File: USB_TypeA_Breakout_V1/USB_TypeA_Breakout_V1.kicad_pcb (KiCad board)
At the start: 2 copper layers, 27 x 20 mm, 2 parts, among them J1 USB_A, J2 Conn_01x04_Male

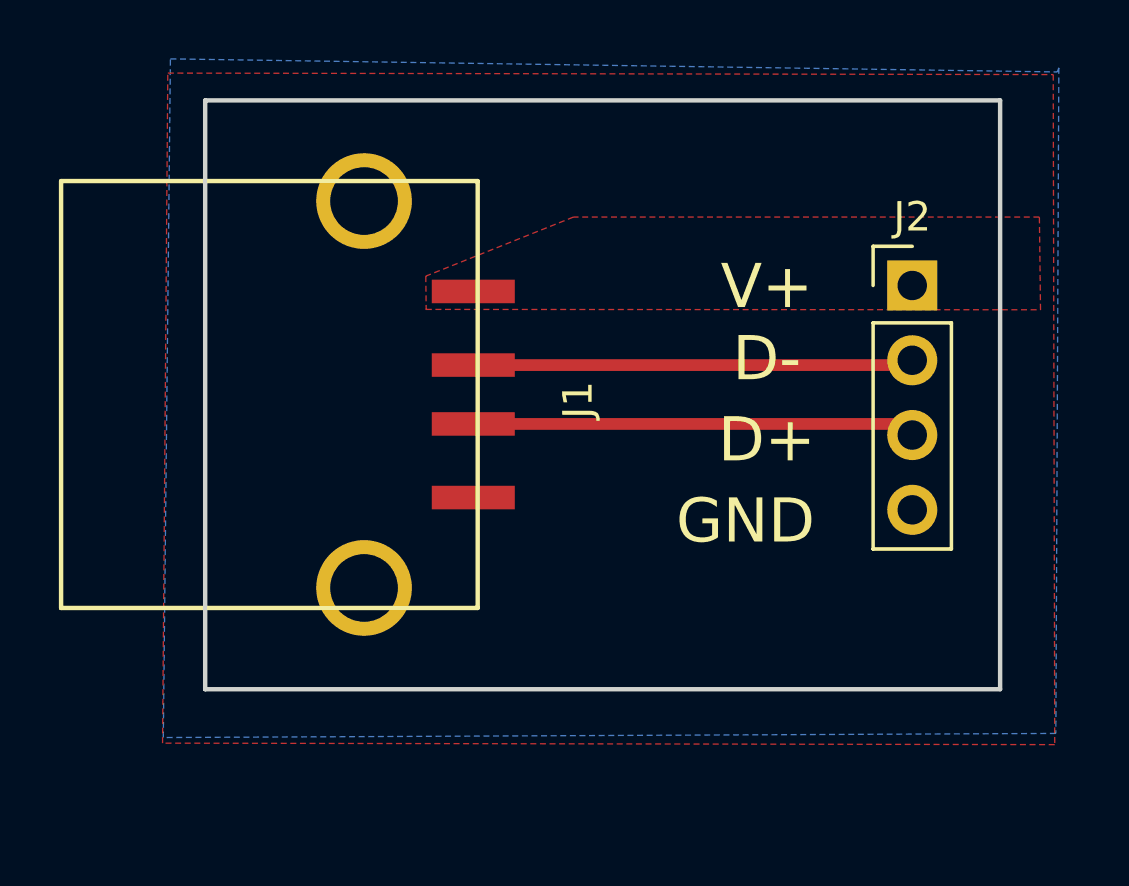
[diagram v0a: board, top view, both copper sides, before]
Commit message: Added rounded corners to PCB layout.
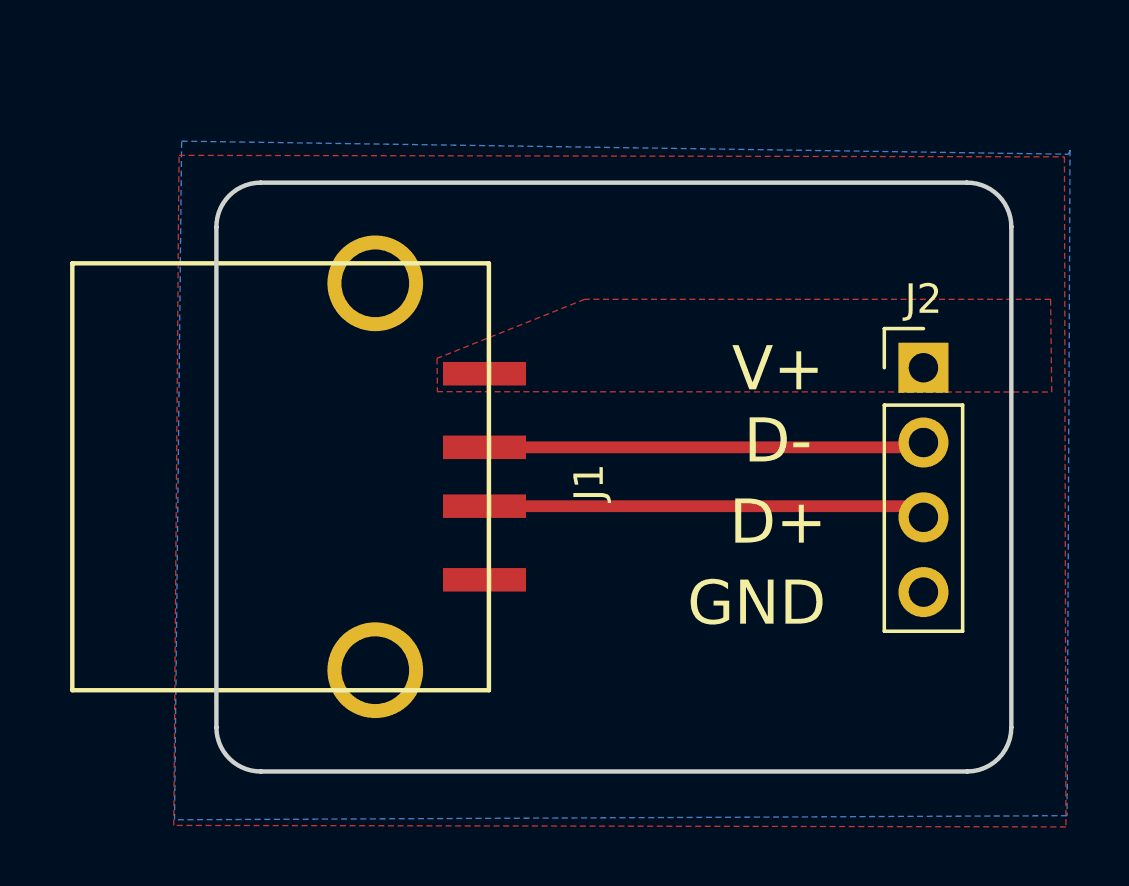
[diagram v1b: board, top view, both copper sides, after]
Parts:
- moved J1 2.82 mm to (121.5, 80.8)
- moved J2 2.82 mm to (136.4, 80.6)
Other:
- outline, holes or cut-outs redrawn
- board text added: "USB Type A Breakout V1"
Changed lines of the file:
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@@
   (general
     (thickness 1.6)
-    (drawings 8)
+    (drawings 13)
     (tracks 4)
     (zones 0)
@@
   )
   (module Custom_Footprints:USB_A_CNC_1002-002-01100 (layer F.Cu)
-    (at 121.158 78.0034 270)
+    (at 121.539 80.7974 270)
     (fp_text reference J1 (at 3.683 -3.556 270) (layer F.SilkS)
       (effects (font (size 1 1) (thickness 0.15)))
@@
   )
   (module Connector_PinHeader_2.54mm:PinHeader_1x04_P2.54mm_Vertical (layer F.Cu)
-    (at 136.0678 77.8002)
+    (at 136.4488 80.5942)
     (descr "Through hole straight pin header, 1x04, 2.54mm pitch, single row")
     (tags "Through hole pin header THT 1x04 2.54mm single row")
@@
     )
   )
-  (gr_line (start 112.0521 71.5137) (end 139.0521 71.5137) (layer Edge.Cuts) (width 0.15))
-  (gr_line (start 139.0521 71.5137) (end 139.0521 91.5137) (layer Edge.Cuts) (width 0.15))
-  (gr_line (start 139.0521 91.5137) (end 112.0521 91.5137) (layer Edge.Cuts) (width 0.15))
-  (gr_line (start 112.0521 91.5137) (end 112.0521 71.5137) (layer Edge.Cuts) (width 0.15))
-  (gr_text GND (at 130.4036 85.8012) (layer F.SilkS)
-    (effects (font (size 1.5 1.5) (thickness 0.3)))
-  )
-  (gr_text D+ (at 131.1275 83.0453) (layer F.SilkS)
-    (effects (font (size 1.5 1.5) (thickness 0.3)))
-  )
-  (gr_text D- (at 131.1275 80.2894) (layer F.SilkS)
-    (effects (font (size 1.5 1.5) (thickness 0.3)))
-  )
-  (gr_text V+ (at 131.1275 77.8383) (layer F.SilkS)
-    (effects (font (size 1.5 1.5) (thickness 0.3)))
-  )
-  (segment (start 135.9046 80.5034) (end 136.0678 80.3402) (width 0.25) (layer F.Cu) (net 2))
-  (segment (start 121.158 80.5034) (end 135.9046 80.5034) (width 0.4) (layer F.Cu) (net 2))
-  (segment (start 135.691 82.5034) (end 136.0678 82.8802) (width 0.25) (layer F.Cu) (net 3))
-  (segment (start 121.158 82.5034) (end 135.691 82.5034) (width 0.4) (layer F.Cu) (net 3))
+  (gr_text "USB Type A\nBreakout V1" (at 126.9238 84.201 90) (layer B.SilkS)
+    (effects (font (size 1.5 1.5) (thickness 0.3)) (justify mirror))
+  )
+  (gr_arc (start 113.9331 75.8077) (end 113.9331 74.3077) (angle -90.43174927) (layer Edge.Cuts) (width 0.15))
+  (gr_arc (start 113.9331 92.8077) (end 112.4331 92.8077) (angle -90.5) (layer Edge.Cuts) (width 0.15))
+  (gr_arc (start 137.9331 75.8077) (end 139.4331 75.8077) (angle -90.42410656) (layer Edge.Cuts) (width 0.15))
+  (gr_arc (start 137.9331 92.8077) (end 137.9331 94.3077) (angle -89.9) (layer Edge.Cuts) (width 0.15))
+  (gr_line (start 113.9331 74.3077) (end 137.921997 74.3077) (layer Edge.Cuts) (width 0.15))
+  (gr_line (start 139.4331 75.8077) (end 139.4331 92.80906) (layer Edge.Cuts) (width 0.15))
+  (gr_line (start 137.9331 94.3077) (end 113.94619 94.3077) (layer Edge.Cuts) (width 0.15))
+  (gr_line (start 112.4331 92.8077) (end 112.4331 75.819003) (layer Edge.Cuts) (width 0.15))
+  (gr_text GND (at 130.7846 88.5952) (layer F.SilkS)
+    (effects (font (size 1.5 1.5) (thickness 0.3)))
+  )
+  (gr_text D+ (at 131.5085 85.8393) (layer F.SilkS)
+    (effects (font (size 1.5 1.5) (thickness 0.3)))
+  )
+  (gr_text D- (at 131.5085 83.0834) (layer F.SilkS)
+    (effects (font (size 1.5 1.5) (thickness 0.3)))
+  )
+  (gr_text V+ (at 131.5085 80.6323) (layer F.SilkS)
+    (effects (font (size 1.5 1.5) (thickness 0.3)))
+  )
+  (segment (start 136.2856 83.2974) (end 136.4488 83.1342) (width 0.25) (layer F.Cu) (net 2))
+  (segment (start 121.539 83.2974) (end 136.2856 83.2974) (width 0.4) (layer F.Cu) (net 2))
+  (segment (start 136.072 85.2974) (end 136.4488 85.6742) (width 0.25) (layer F.Cu) (net 3))
+  (segment (start 121.539 85.2974) (end 136.072 85.2974) (width 0.4) (layer F.Cu) (net 3))
   (zone (net 1) (net_name "Net-(J1-Pad1)") (layer F.Cu) (hatch edge 0.508)
     (priority 1)
@@
     (polygon
       (pts
-        (xy 119.5451 78.613) (xy 140.4239 78.6257) (xy 140.3858 75.4761) (xy 124.5616 75.4761) (xy 119.5451 77.4827)
-        (xy 119.5578 78.613)
+        (xy 119.9261 81.407) (xy 140.8049 81.4197) (xy 140.7668 78.2701) (xy 124.9426 78.2701) (xy 119.9261 80.2767)
+        (xy 119.9388 81.407)
       )
     )
@@
     (polygon
       (pts
-        (xy 140.8557 70.6374) (xy 140.9065 93.3958) (xy 110.6043 93.345) (xy 110.7821 70.5866)
+        (xy 141.2367 73.4314) (xy 141.2875 96.1898) (xy 110.9853 96.139) (xy 111.1631 73.3806)
       )
     )
@@
     (polygon
       (pts
-        (xy 141.0462 70.4088) (xy 140.9446 93.0148) (xy 110.6297 93.1545) (xy 110.871 70.104) (xy 140.9954 70.5485)
+        (xy 141.4272 73.2028) (xy 141.3256 95.8088) (xy 111.0107 95.9485) (xy 111.252 72.898) (xy 141.3764 73.3425)
       )
     )
